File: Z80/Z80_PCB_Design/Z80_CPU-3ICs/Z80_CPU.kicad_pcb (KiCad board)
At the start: 2 copper layers, 95 x 95 mm, 37 parts, among them J1 USB_B, U1 Z80CPU, U2 AS6C4008-55PCN, U3 4.9152 MHz, U4 CY8C5267AXI-LP051, Y1 32.768KHz

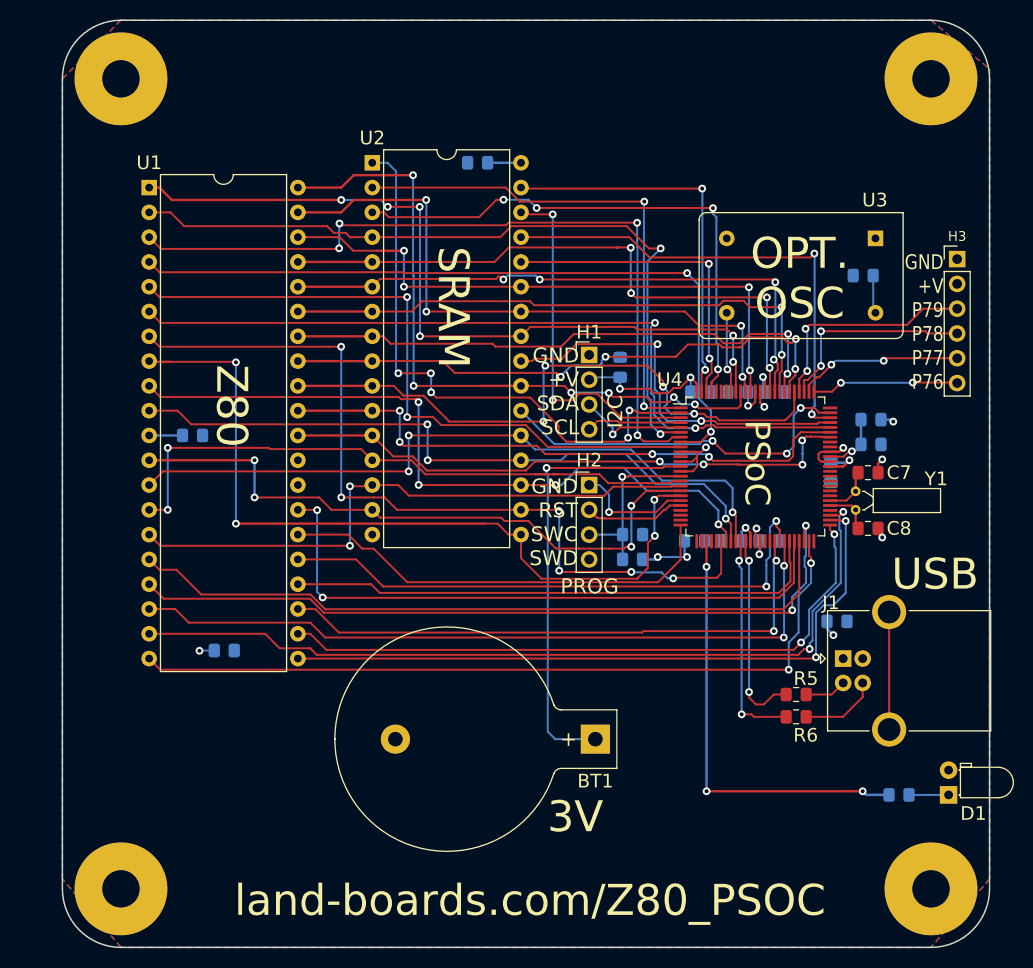
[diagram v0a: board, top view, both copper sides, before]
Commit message: Z80 Front Panel Design
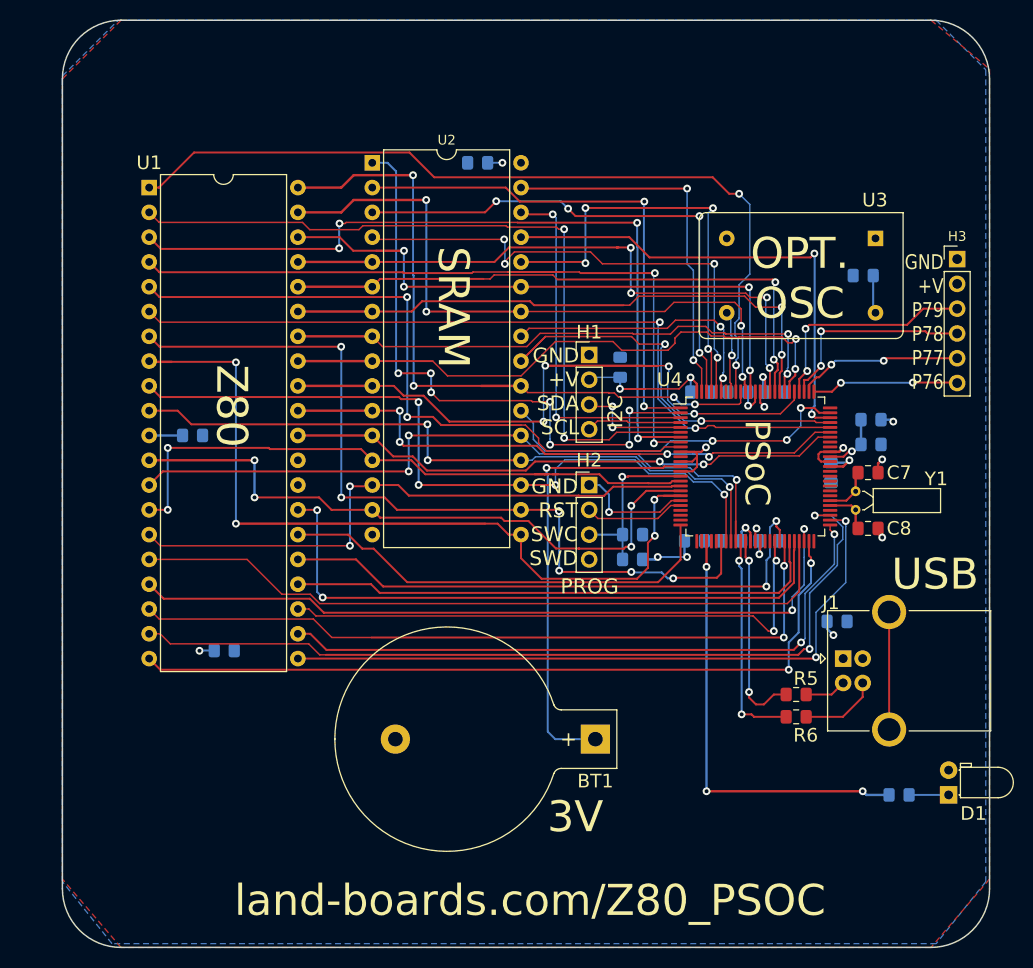
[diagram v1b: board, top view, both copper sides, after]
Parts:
- removed MTG1, MTG2, MTG3, MTG?1: MTG_HOLE, LandBoards_MountHoles:MTG-6-32
- U2: value AS6C4008-55PCN -> my_components_AS6C4008_PWR
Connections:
- U2 pad 25: /CPUA11 -> /SRAMA11
- U2 pad 28: /SRAMA14 -> /SRAMA13
- U2 pad 3: /SRAMA13 -> /SRAMA14
- U2 pad 4: /CPUA12 -> /SRAMA12
- U4 pad 95: (no net) -> /SRAMA11
- U4 pad 96: (no net) -> /SRAMA12
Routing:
- net /SRAMA12: track 0.00 -> 52.1 mm, vias 0 -> 4
- net /SRAMA11: track 0.00 -> 28.3 mm, vias 0 -> 2
- net /CPUA2: track 64.4 -> 86.7 mm
- net /SRAMA14: track 32.8 -> 52.9 mm, vias 2 -> 4
- net /SRAMA13: track 55.5 -> 44.5 mm
- net /CPUA11: track 80.5 -> 85.3 mm, vias 6 -> 2
- net /CPUA13: track 79.9 -> 84.5 mm
- net /~MEMRD: track 40.1 -> 43.7 mm
- net /CPUD5: track 73.5 -> 76.5 mm
- net /SRAMA18: track 60.0 -> 62.8 mm, vias 5 -> 7
- net /CPUA14: track 76.4 -> 78.4 mm
- net /CPUA9: track 64.9 -> 66.7 mm
- net /~MREQ: track 85.9 -> 87.7 mm
- net /CPUA0: track 59.3 -> 57.7 mm, vias 4 -> 2
- net /CPUA1: track 60.7 -> 59.4 mm
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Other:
- rule trace_min: 0.2 -> 0.1524

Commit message: Front panel design
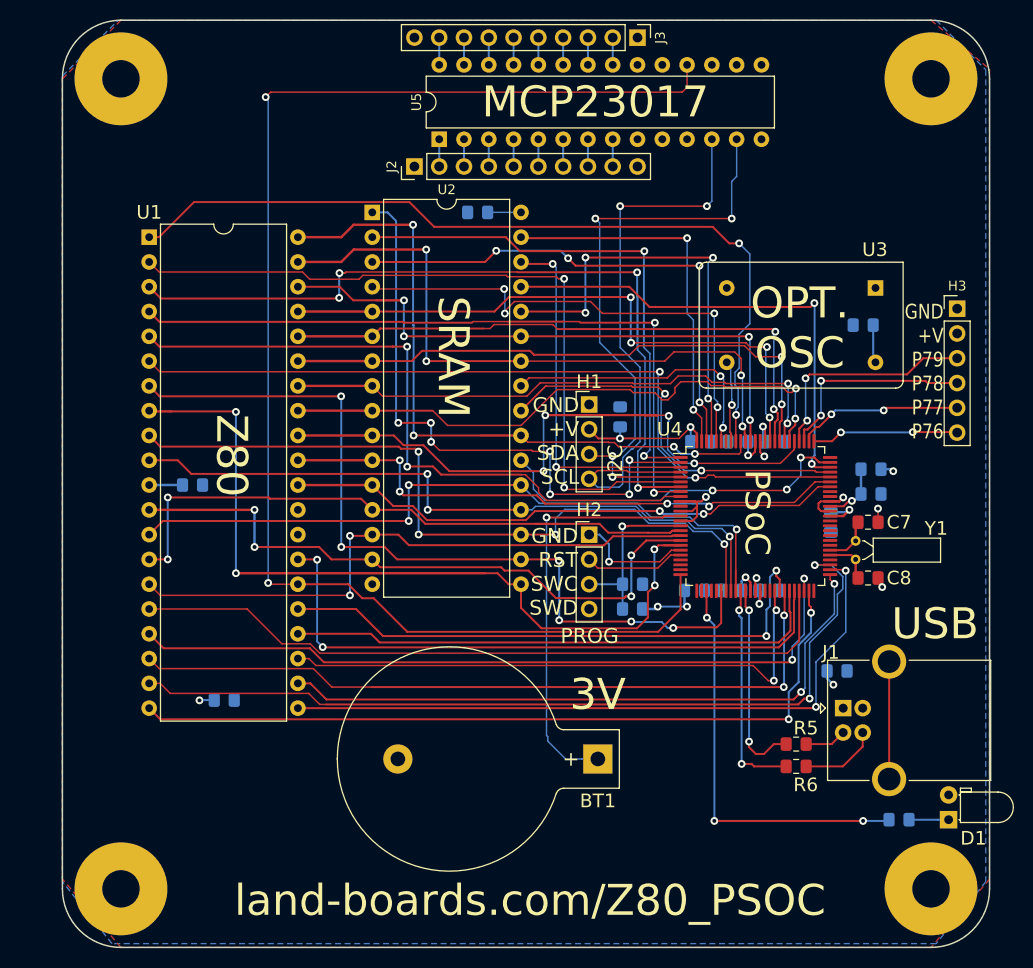
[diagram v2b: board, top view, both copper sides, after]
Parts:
- added J2: Conn_01x10, Connector_PinHeader_2.54mm:PinHeader_1x10_P2.54mm_Vertical, F.Cu at (36.1, 15.0)
- added J3: Conn_01x10, Connector_PinHeader_2.54mm:PinHeader_1x10_P2.54mm_Vertical, F.Cu at (58.9, 1.78)
- added MTG1: MTG_HOLE, LandBoards_MountHoles:MTG-6-32, F.Cu at (6.00, 6.00)
- added MTG2: MTG_HOLE, LandBoards_MountHoles:MTG-6-32, F.Cu at (89.0, 6.00)
- added MTG3: MTG_HOLE, LandBoards_MountHoles:MTG-6-32, F.Cu at (6.00, 89.0)
- added MTG?1: MTG_HOLE, LandBoards_MountHoles:MTG-6-32, F.Cu at (89.0, 89.0)
- added U5: MCP23017_SP, Package_DIP:DIP-28_W7.62mm, F.Cu at (38.6, 12.2)
- moved R5 5.08 mm to (75.2, 74.2)
- moved C5 5.08 mm to (78.7, 51.4)
- moved C7 5.08 mm to (82.5, 51.4)
- moved R4 5.08 mm to (58.4, 60.3)
- moved C14 5.08 mm to (82.1, 31.2)
- moved H3 5.08 mm to (91.7, 29.6)
- moved U1 5.08 mm to (8.89, 22.2)
- moved C1 5.08 mm to (58.4, 57.8)
- moved C10 5.08 mm to (13.3, 47.6)
- moved C11 5.08 mm to (79.4, 66.7)
- moved C12 5.08 mm to (65.4, 43.2)
- moved C13 5.08 mm to (42.5, 19.7)
- moved C15 5.08 mm to (57.1, 40.6)
- moved C17 5.08 mm to (69.2, 43.2)
- moved C18 5.08 mm to (68.6, 58.4)
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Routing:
- net /~CPURST: track 45.7 -> 144.6 mm, vias 0 -> 2
- net /SCL: track 9.78 -> 59.8 mm, vias 0 -> 2
- net /SDA: track 11.6 -> 61.2 mm, vias 2 -> 4
- net Net-(BT1-Pad1): track 46.1 -> 42.7 mm
- net Net-(J2-Pad9): track 0.00 -> 2.79 mm
- net Net-(J2-Pad8): track 0.00 -> 2.79 mm
- net Net-(J2-Pad7): track 0.00 -> 2.79 mm
- net Net-(J2-Pad6): track 0.00 -> 2.79 mm
- net Net-(J2-Pad5): track 0.00 -> 2.79 mm
- net Net-(J2-Pad4): track 0.00 -> 2.79 mm
- net Net-(J2-Pad3): track 0.00 -> 2.79 mm
- net Net-(J2-Pad2): track 0.00 -> 2.79 mm
- net Net-(J3-Pad9): track 0.00 -> 2.79 mm
- net Net-(J3-Pad8): track 0.00 -> 2.79 mm
- net Net-(J3-Pad7): track 0.00 -> 2.79 mm
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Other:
- board text added: "MCP23017"

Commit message: z80 cpu legends
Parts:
- moved J2 22.9 mm to (59.0, 15.0), turned to 270 degrees
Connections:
- net Net-(J3-Pad2) renamed /GPA0
- net Net-(J3-Pad9) renamed /GPA7
- J2 pad 1: +5V -> GND
- J2 pad 10: GND -> +5V
- J2 pad 2: Net-(J2-Pad2) -> /GPB7
- J2 pad 9: Net-(J2-Pad9) -> /GPB0
- J3 pad 1: +5V -> GND
- J3 pad 10: GND -> +5V
- U5 pad 1: Net-(J2-Pad2) -> /GPB0
- U5 pad 2: Net-(J2-Pad3) -> Net-(J2-Pad8)
- U5 pad 3: Net-(J2-Pad4) -> Net-(J2-Pad7)
- U5 pad 4: Net-(J2-Pad5) -> Net-(J2-Pad6)
- U5 pad 5: Net-(J2-Pad6) -> Net-(J2-Pad5)
- U5 pad 6: Net-(J2-Pad7) -> Net-(J2-Pad4)
- U5 pad 7: Net-(J2-Pad8) -> Net-(J2-Pad3)
- U5 pad 8: Net-(J2-Pad9) -> /GPB7
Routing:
- net Net-(J2-Pad9): track 2.79 -> 0.00 mm
- net Net-(J2-Pad2): track 2.79 -> 0.00 mm
- net /GPB7: track 0.00 -> 2.79 mm
- net /GPB0: track 0.00 -> 2.79 mm
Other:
- board text added: "512KB SRAM"
- board text added: "VCC_A0_A7_GND"
- board text added: "VCC_B7_B0_GND"
- board text added: "Z80 CPU"
- board text removed: "SRAM"
- board text removed: "Z80"

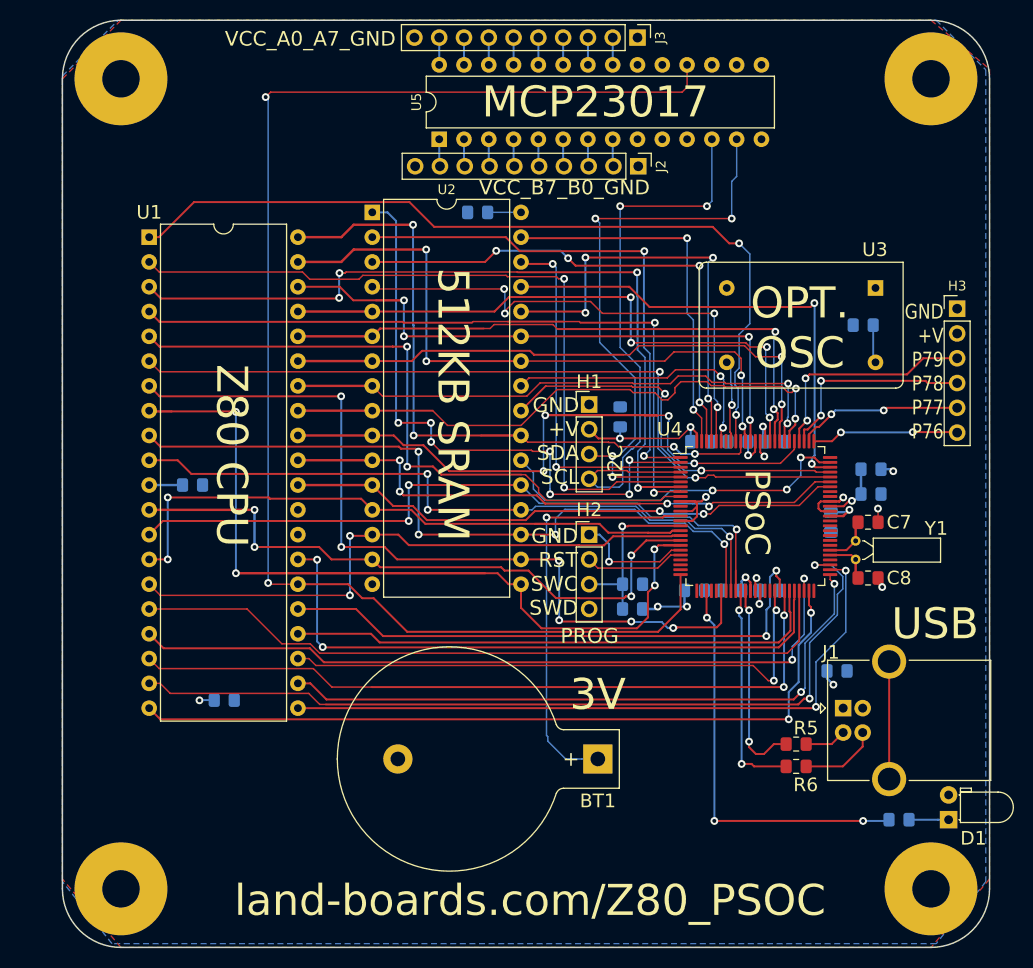
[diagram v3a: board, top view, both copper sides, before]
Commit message: Added I2C interface to Z80 CPU
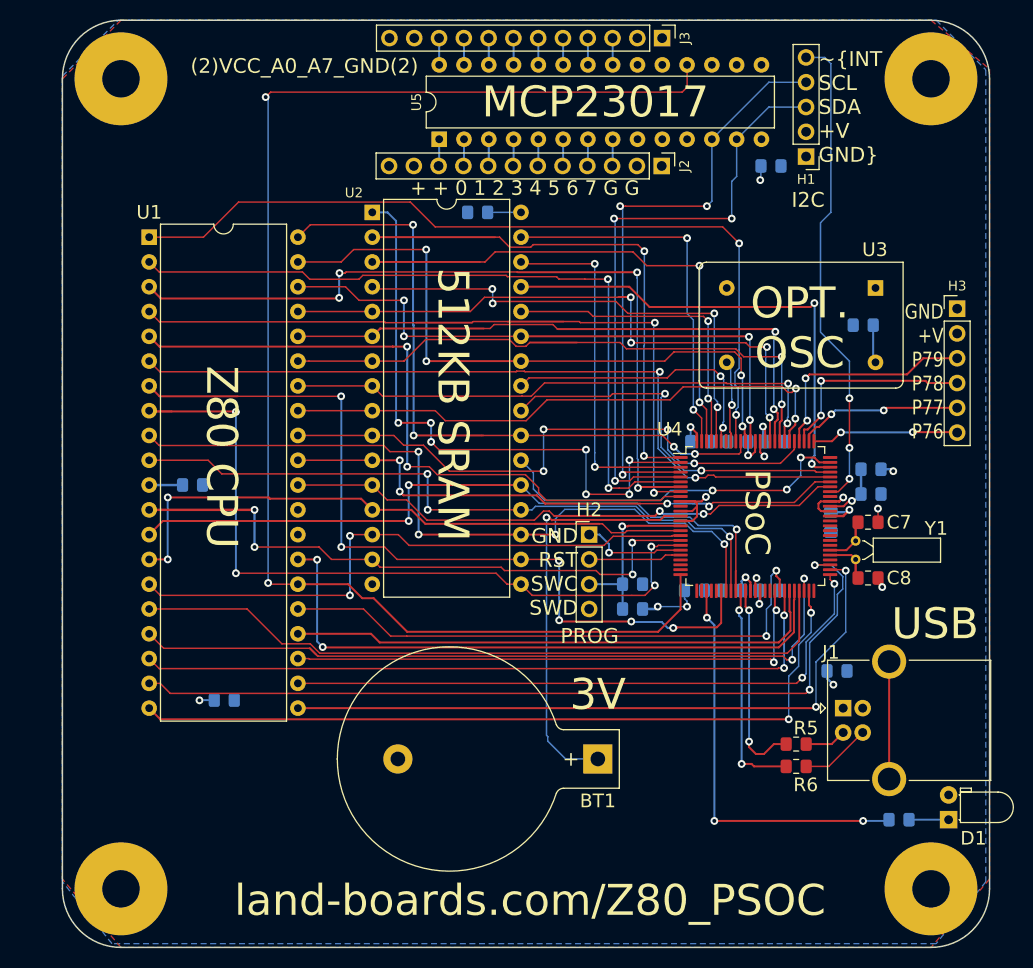
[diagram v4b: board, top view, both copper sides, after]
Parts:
- H1: value Conn_01x04 -> Conn_01x05; footprint Connector_PinHeader_2.54mm:PinHeader_1x04_P2.54mm_Vertical -> Connector_PinHeader_2.54mm:PinHeader_1x05_P2.54mm_Vertical
- J2, J3: value Conn_01x10 -> Conn_01x12; footprint Connector_PinHeader_2.54mm:PinHeader_1x10_P2.54mm_Vertical -> Connector_PinHeader_2.54mm:PinHeader_1x12_P2.54mm_Vertical
- U2: value my_components_AS6C4008_PWR -> AS6C4008
- moved H1 33.8 mm to (76.2, 14.0), turned to 180 degrees
- moved C15 30.0 mm to (72.6, 14.9), turned to 180 degrees
- moved J3 2.52 mm to (61.5, 1.83)
- moved J2 2.40 mm to (61.4, 14.9)
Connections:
- J2 pad 10: +5V -> /GPB0
- J2 pad 2: /GPB7 -> GND
- J2 pad 3: Net-(J2-Pad3) -> /GPB7
- J2 pad 4: Net-(J2-Pad4) -> /GPB6
- J2 pad 5: Net-(J2-Pad5) -> /GPB5
- J2 pad 6: Net-(J2-Pad6) -> /GPB4
- J2 pad 7: Net-(J2-Pad7) -> /GPB3
- J2 pad 8: Net-(J2-Pad8) -> /GPB2
- J2 pad 9: /GPB0 -> /GPB1
- J3 pad 10: +5V -> /GPA7
- J3 pad 2: /GPA0 -> GND
- J3 pad 3: Net-(J3-Pad3) -> /GPA0
- J3 pad 4: Net-(J3-Pad4) -> /GPA1
- J3 pad 5: Net-(J3-Pad5) -> /GPA2
- J3 pad 6: Net-(J3-Pad6) -> /GPA3
- J3 pad 7: Net-(J3-Pad7) -> /GPA4
- J3 pad 8: Net-(J3-Pad8) -> /GPA5
- J3 pad 9: /GPA7 -> /GPA6
- U4 pad 68: (no net) -> /~I2CINT
- U5 pad 2: Net-(J2-Pad8) -> /GPB1
- U5 pad 22: Net-(J3-Pad3) -> /GPA1
- U5 pad 23: Net-(J3-Pad4) -> /GPA2
- U5 pad 24: Net-(J3-Pad5) -> /GPA3
- U5 pad 25: Net-(J3-Pad6) -> /GPA4
- U5 pad 26: Net-(J3-Pad7) -> /GPA5
- U5 pad 27: Net-(J3-Pad8) -> /GPA6
- U5 pad 3: Net-(J2-Pad7) -> /GPB2
- U5 pad 4: Net-(J2-Pad6) -> /GPB3
- U5 pad 5: Net-(J2-Pad5) -> /GPB4
- U5 pad 6: Net-(J2-Pad4) -> /GPB5
- U5 pad 7: Net-(J2-Pad3) -> /GPB6
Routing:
- net /~I2CINT: track 0.00 -> 49.6 mm, vias 0 -> 3
- net /CPUA2: track 86.7 -> 60.7 mm
- net +5V: track 46.4 -> 32.9 mm
- net /SRAMA13: track 44.5 -> 32.0 mm, vias 4 -> 2
- net /CPUA10: track 69.4 -> 76.6 mm
- net /CPUD3: track 83.8 -> 76.9 mm
- net /CPUA5: track 59.8 -> 65.1 mm
- net /~MEMRD: track 43.7 -> 39.5 mm
- net Net-(J2-Pad8): track 2.79 -> 0.00 mm
- net Net-(J2-Pad7): track 2.79 -> 0.00 mm
- net Net-(J2-Pad6): track 2.79 -> 0.00 mm
- net Net-(J2-Pad5): track 2.79 -> 0.00 mm
- net Net-(J2-Pad4): track 2.79 -> 0.00 mm
- net Net-(J2-Pad3): track 2.79 -> 0.00 mm
- net /GPB6: track 0.00 -> 2.79 mm
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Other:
- board text added: "(2)VCC_A0_A7_GND(2)"
- board text added: "+ + 0 1 2 3 4 5 6 7 G G"
- board text added: "~INT SCL SDA +V GND"
- board text removed: "GND +V SDA SCL"
- board text removed: "VCC_A0_A7_GND"
- board text removed: "VCC_B7_B0_GND"

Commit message: z80
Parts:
- added C16: 10pF, Capacitor_SMD:C_0805_2012Metric_Pad1.15x1.40mm_HandSolder, B.Cu at (88.1, 52.1)
- added J4: Conn_01x02, Connector_PinHeader_2.54mm:PinHeader_1x02_P2.54mm_Vertical, F.Cu at (93.2, 49.3)
- added R1: 2.2K, Resistor_SMD:R_0805_2012Metric_Pad1.15x1.40mm_HandSolder, B.Cu at (79.4, 8.89)
- added R2: 2.2K, Resistor_SMD:R_0805_2012Metric_Pad1.15x1.40mm_HandSolder, B.Cu at (79.4, 6.35)
- added R3: 2.2K, Resistor_SMD:R_0805_2012Metric_Pad1.15x1.40mm_HandSolder, B.Cu at (79.4, 3.81)
- added R8: 2.2K, Resistor_SMD:R_0805_2012Metric_Pad1.15x1.40mm_HandSolder, B.Cu at (88.1, 48.3)
- added R9: 2.2K, Resistor_SMD:R_0805_2012Metric_Pad1.15x1.40mm_HandSolder, B.Cu at (88.1, 50.3)
- moved L1 2.84 mm to (84.6, 48.3), turned to 90 degrees
- moved C14 1.24 mm to (83.2, 31.8), turned to 270 degrees
- moved C4 0.42 mm to (82.5, 48.3), turned to 90 degrees
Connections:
- U4 pad 94: (no net) -> /DAC_OUT
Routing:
- net /DAC_OUT: track 0.00 -> 32.1 mm, vias 0 -> 5
- net /CPUA1: track 59.4 -> 73.1 mm
- net (no net): track 0.05 -> 11.8 mm, vias 0 -> 7
- net Net-(C16-Pad2): track 0.00 -> 8.29 mm
- net /~I2CINT: track 49.6 -> 57.5 mm, vias 3 -> 2
- net +5V: track 32.9 -> 39.8 mm
- net /CPUA5: track 65.1 -> 60.0 mm
- net /SDA: track 62.7 -> 64.8 mm
- net /SCL: track 61.7 -> 63.9 mm
- net /CPUA3: track 59.0 -> 60.9 mm, vias 2 -> 4
- net /P76: track 15.1 -> 16.9 mm, vias 2 -> 0
- net /~MEMRD: track 39.5 -> 37.8 mm
- net GND: track 19.9 -> 18.4 mm
- net /CPUA4: track 57.3 -> 58.8 mm
- net /CPUA6: track 61.3 -> 62.6 mm
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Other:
- board text added: "(2)VCC_A7_A0_GND(2)"
- board text added: "GND"
- board text added: "GPA"
- board text added: "GPB"
- board text added: "VO"
- board text removed: "(2)VCC_A0_A7_GND(2)"
